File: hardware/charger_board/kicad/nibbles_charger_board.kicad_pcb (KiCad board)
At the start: 4 copper layers, 54 x 33 mm, 34 parts, among them J21 XT30 (from the power board: i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, J22 XT30 (to the power board: bat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, J23 JST-GH 6 (to the power board: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, J4 NTC 103AT on the cells, U2 BQ25798RQMR

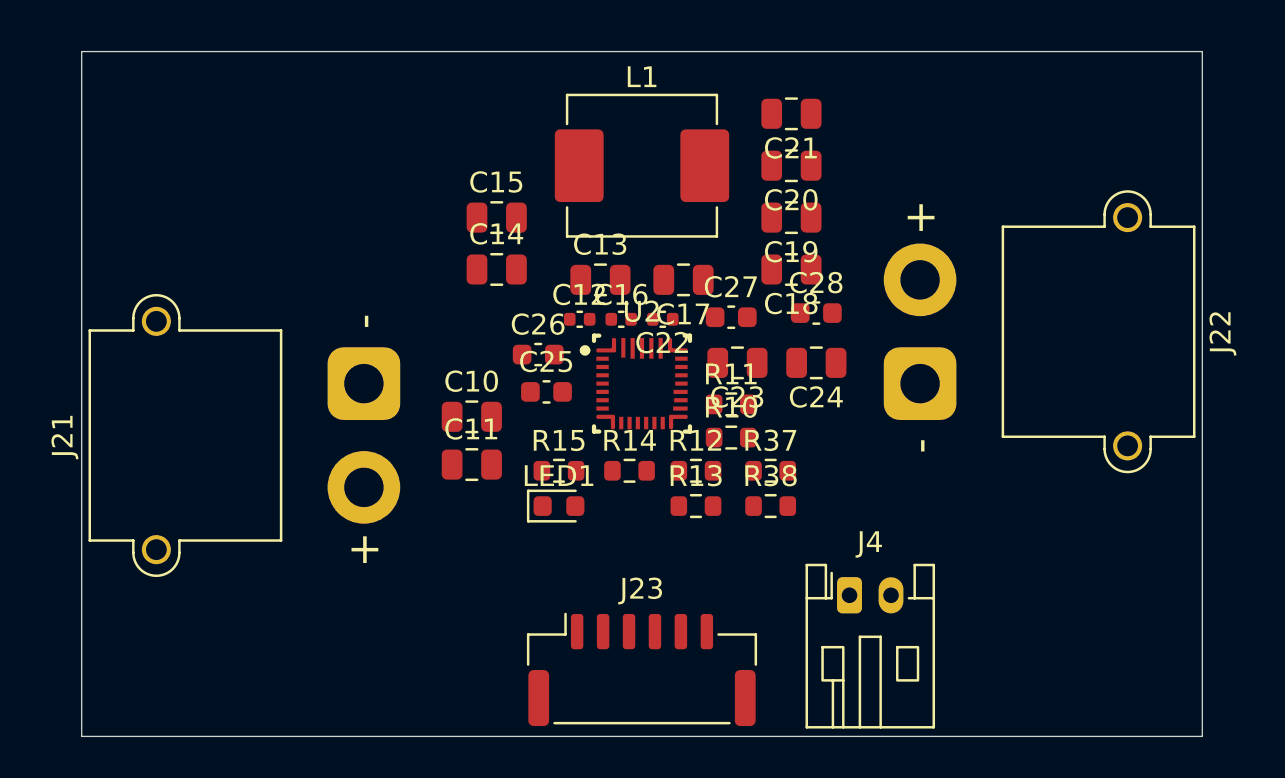
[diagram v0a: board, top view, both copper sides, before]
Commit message: Combined power + charger project, charger schematic wired, 30 mm charger board
- hardware/power_charger_board: a copy of the power board with the charger
  added, for laying both out as one board. One schematic sheet (charger as
  section 4), charger parts on their own 22 x 30 mm outline beside the
  power board, the XT30s that linked the boards (J10, J11, J21, J22)
  removed, 4 copper layers, a Charger net class (3 mm) on PMID, SYS, SW1
  and SW2.
- Charger schematic (standalone and combined) redrawn with the parts wired
  to the BQ25798's pins; short two-pin nets now use KiCad's automatic
  names, renamed to match in the boards.
- Standalone charger board: 54 x 30 mm outline for the narrow enclosure,
  inductor pulled in, NTC connector moved; KXUSBC2 noted as a layout
  reference.
- Generator: can build one board; refuses the hand-edited power and
  charger boards unless forced; pre-defined track and via sizes.

Co-Authored-By: Claude Opus 5.5 <noreply@anthropic.com>
Claude-Session: https://claude.ai/code/session_01UUhpevE9ZSCJvyu3edQmf9
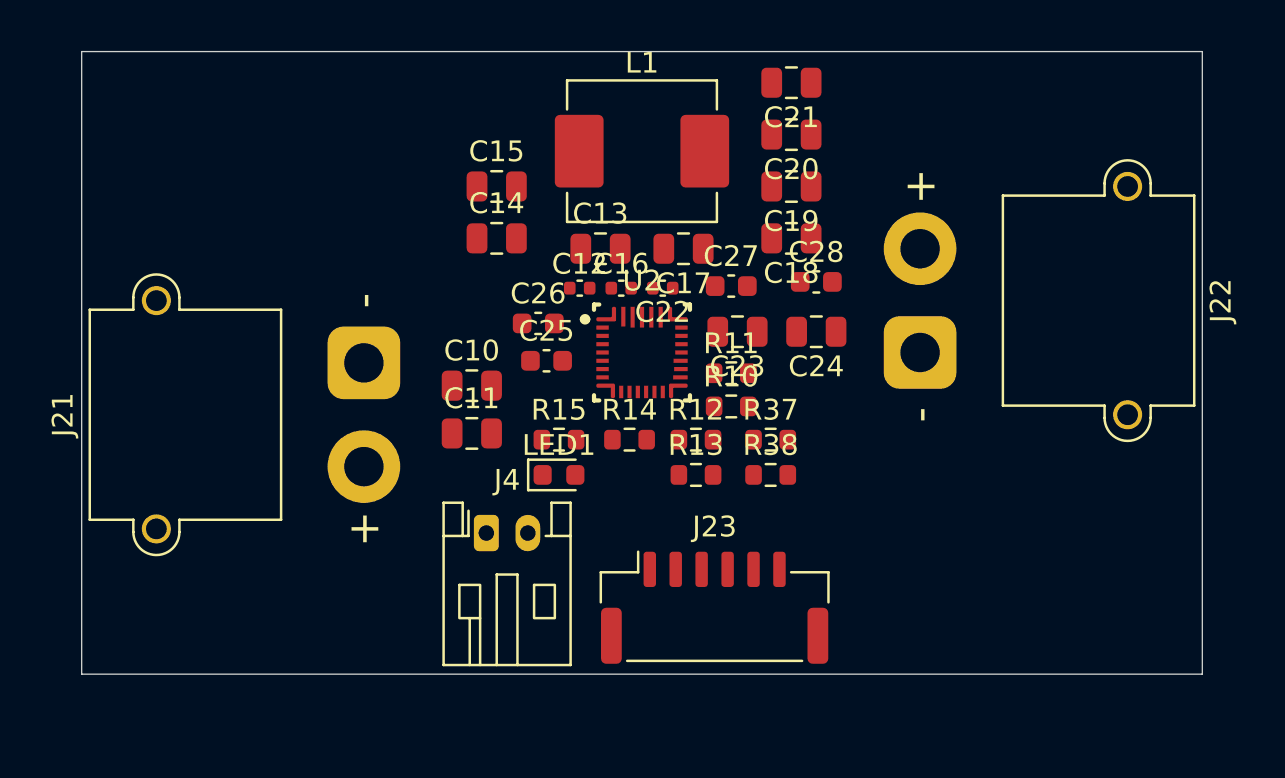
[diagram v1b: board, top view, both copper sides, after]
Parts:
- moved J4 17.8 mm to (69.5, 73.2)
- moved J23 4.61 mm to (80.5, 76.8)
- moved C10 1.50 mm to (68.8, 66.1)
- moved R10 1.50 mm to (81.3, 67.1)
- moved C11 1.50 mm to (68.8, 68.4)
- moved C12 1.50 mm to (74.0, 61.4)
- moved C13 1.50 mm to (75.0, 59.5)
- moved C14 1.50 mm to (70.0, 59.0)
- moved C15 1.50 mm to (70.0, 56.5)
- moved C16 1.50 mm to (76.0, 61.4)
- moved C17 1.50 mm to (79.0, 59.5)
- moved C18 1.50 mm to (84.2, 59.0)
- moved C19 1.50 mm to (84.2, 56.5)
- moved C20 1.50 mm to (84.2, 54.0)
- moved C21 1.50 mm to (84.2, 51.5)
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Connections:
- net BATP renamed Net-(U2-BATP)
- net BTST1 renamed Net-(U2-BTST1)
- net BTST2 renamed Net-(U2-BTST2)
- net CHG_CE renamed Net-(U2-CE_N)
- net CHG_ILIM renamed Net-(U2-ILIM_HIZ)
- net CHG_PROG renamed Net-(U2-PROG)
- net CHG_STAT renamed Net-(LED1-C)
- net CHG_TS renamed Net-(U2-TS)
- net SDRV renamed Net-(U2-SDRV)
- net STAT_LED renamed Net-(LED1-A)
- U2 pad 6: (no net) -> unconnected-(U2-D+-Pad6)
- U2 pad 7: (no net) -> unconnected-(U2-D--Pad7)
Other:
- board size 54 x 33 mm -> 54 x 30 mm
- board text added: "Placeholder outline 54 x 30 mm: resize to the enclosure. Left edge: input from the power board (J21). Right edge: battery (J22). Bottom edge: NTC on the cells (J4), I2C (J23). Short side kept to 30 mm for the enclosure."
- board text removed: "Placeholder outline 54 x 33 mm: resize to the enclosure. Left edge: input from the power board (J21). Right edge: battery (J22). Bottom edge: I2C (J23), NTC on the cells (J4)."
